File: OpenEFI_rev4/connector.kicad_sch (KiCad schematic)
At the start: 58 parts, among them J6 1241434-1, Q10 PMN30XPX, Q20 PMN30XPX, Q5 SS8050, Q6 IRLZ44N, Q7 IRLZ44N, U14 MIC5205-3.3YM5, U16 TPS5430DDA, U17 L78M05ABDT-TR, U4 AMS1117-3.3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

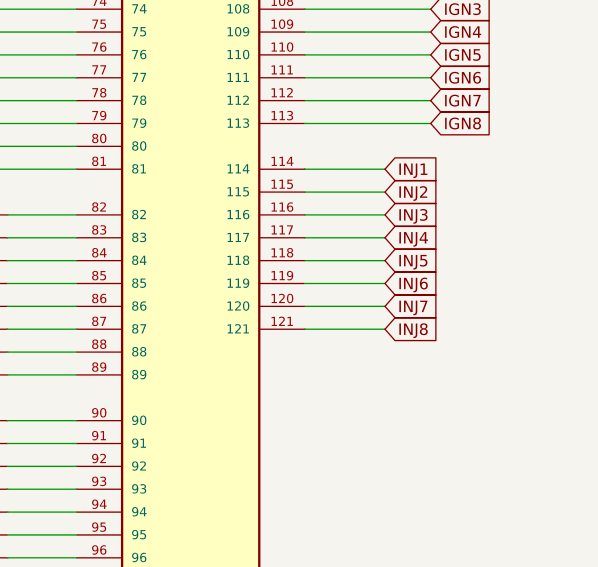
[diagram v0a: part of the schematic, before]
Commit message: Rev4: add all MCU signals
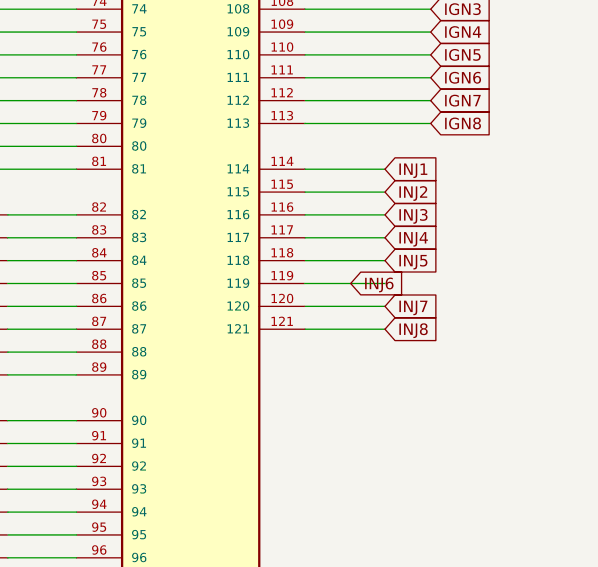
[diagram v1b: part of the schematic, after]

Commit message: Rev4 WIP LCSC assigments
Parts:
- C33, C60, C61: LCSC (none) -> C1622
- C42: LCSC null -> C141427
- FL1: LCSC (none) -> C161093
- R2: LCSC (none) -> C25804
- R2: LCSC C2933197 -> C25804
- R33: LCSC (none) -> C109317
- U14: LCSC (none) -> C70431
- U16: LCSC (none) -> C9864
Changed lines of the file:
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@@
+      (effects (font (size 1.27 1.27)) hide)
+    )
+    (property "LCSC" "C1622" (at 55.6768 160.1216 0)
       (effects (font (size 1.27 1.27)) hide)
     )
@@
       (effects (font (size 1.27 1.27)) hide)
     )
+    (property "LCSC" "C109317" (at 31.75 60.96 0)
+      (effects (font (size 1.27 1.27)) hide)
+    )
     (pin "1")
     (pin "2")
@@
     )
     (property "Description" "" (at 40.64 90.17 0)
+      (effects (font (size 1.27 1.27)) hide)
+    )
+    (property "LCSC" "C9864" (at 40.64 77.47 0)
       (effects (font (size 1.27 1.27)) hide)
     )
@@
       (effects (font (size 1.27 1.27)) (justify bottom) hide)
     )
+    (property "LCSC" "C161093" (at 133.8072 172.72 0)
+      (effects (font (size 1.27 1.27)) hide)
+    )
     (pin "1")
     (pin "2")
@@
       (effects (font (size 1.27 1.27)) hide)
     )
+    (property "LCSC" "C25804" (at 83.82 90.17 0)
+      (effects (font (size 1.27 1.27)) hide)
+    )
     (pin "1")
     (pin "2")
@@
     )
     (property "Description" "" (at 254 154.94 0)
+      (effects (font (size 1.27 1.27)) hide)
+    )
+    (property "LCSC" "C1622" (at 256.3368 153.7716 0)
       (effects (font (size 1.27 1.27)) hide)
     )
@@
       (effects (font (size 1.27 1.27)) hide)
     )
-    (property "LCSC" "C2933197" (at 81.28 99.06 90)
+    (property "LCSC" "C25804" (at 81.28 99.06 90)
       (effects (font (size 0.889 0.889)) hide)
     )
@@
       (effects (font (size 1.27 1.27)) hide)
     )
-    (property "LCSC" "null" (at 87.63 90.17 0)
+    (property "LCSC" "C141427" (at 87.63 90.17 0)
       (effects (font (size 0.889 0.889)) hide)
     )
@@
     )
     (property "Description" "" (at 241.3 149.86 0)
+      (effects (font (size 1.27 1.27)) hide)
+    )
+    (property "LCSC" "C70431" (at 241.3 140.97 0)
       (effects (font (size 1.27 1.27)) hide)
     )
@@
       (effects (font (size 1.27 1.27)) hide)
     )
+    (property "LCSC" "C1622" (at 228.3968 153.7716 0)
+      (effects (font (size 1.27 1.27)) hide)
+    )

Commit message: update footprints
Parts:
- J6, JP10, JP11, JP12, JP4: now left out of the parts list
